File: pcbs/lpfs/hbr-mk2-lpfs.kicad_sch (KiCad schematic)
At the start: 52 parts, among them J1 Conn_01x03, J10 Conn_01x01, J2 Conn_01x02, J3 Conn_01x06, J4 Conn_01x04, J5 Conn_01x01, J6 Conn_Coaxial, J7 Conn_Coaxial, J8 Conn_Coaxial, J9 Conn_Coaxial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

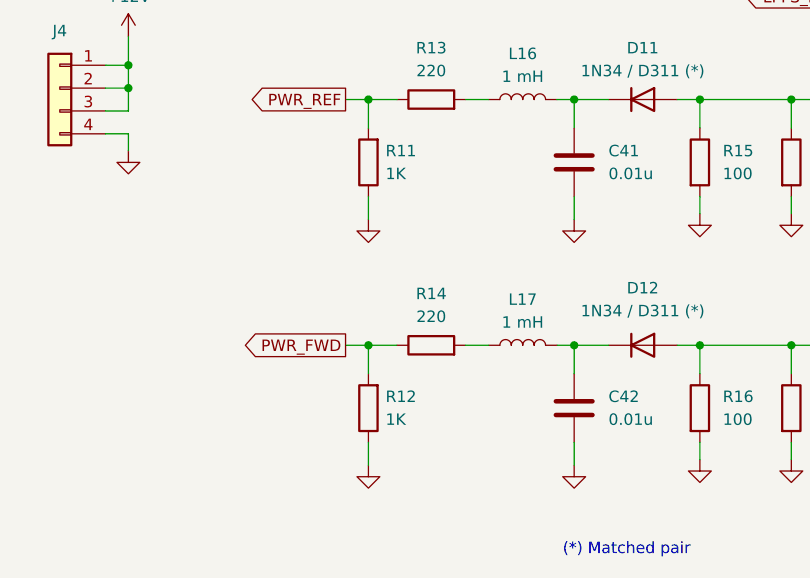
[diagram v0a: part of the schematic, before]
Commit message: LPFs: update R11,R12 values
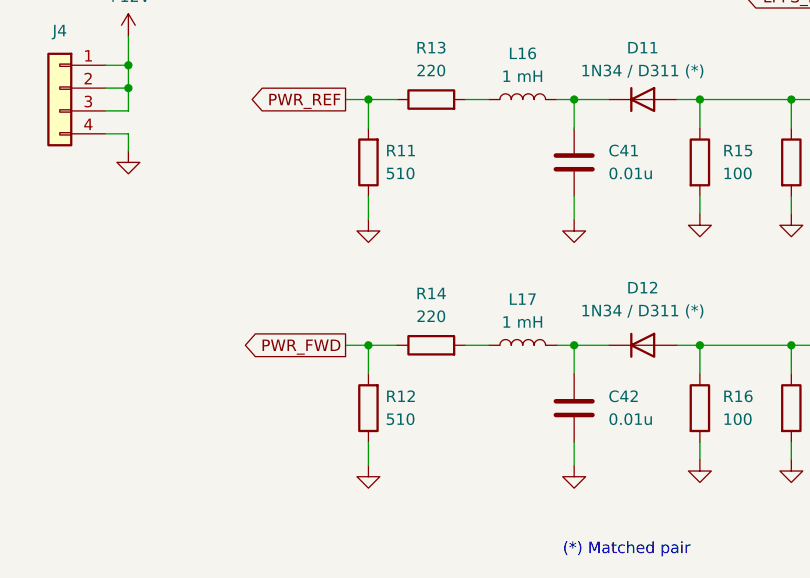
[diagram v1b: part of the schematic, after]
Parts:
- R11, R12: value 1K -> 510
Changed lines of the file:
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@@
       (effects (font (size 1.27 1.27)) (justify right))
     )
-    (property "Value" "1K" (at 66.675 151.765 0)
+    (property "Value" "510" (at 66.675 151.765 0)
       (effects (font (size 1.27 1.27)) (justify right))
     )
@@
       (effects (font (size 1.27 1.27)) (justify right))
     )
-    (property "Value" "1K" (at 66.675 179.07 0)
+    (property "Value" "510" (at 66.675 179.07 0)
       (effects (font (size 1.27 1.27)) (justify right))
     )

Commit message: Various minor improvements
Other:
- note added: "<- Hint: solder a 22p capacitor here if you encounter UHF oscillations during transmit (it looks like high current consumption when nothing is tranmitted). Don't worry, this will not affect the sensitivity."
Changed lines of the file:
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@@
+    (effects (font (size 1.27 1.27)) (justify left bottom))
+  )
+  (text "<- Hint: solder a 22p capacitor here\n    if you encounter UHF oscillations\n    during transmit (it looks like high\n    current consumption when nothing\n    is tranmitted). Don't worry, this will\n    not affect the sensitivity."
+    (at 55.245 104.775 0)
     (effects (font (size 1.27 1.27)) (justify left bottom))
   )
